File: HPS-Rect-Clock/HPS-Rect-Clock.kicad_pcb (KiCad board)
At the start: 2 copper layers, 140 x 90 mm, 58 parts, among them J1 Conn_01x06, J2 Power_inlet_vertical, J3 Conn_02x03_Odd_Even, SW1 Omron_B3F_SPST, SW2 Omron_B3F_SPST, SW3 Omron_B3F_SPST, SW4 Omron_B3F_SPST, SW5 Omron_B3F_SPST, U1 DS1307_DIP-8, U2 ATmega328-PU, U3 L7805, Y1 Crystal_16MHz, Y2 Crystal_32768Hz

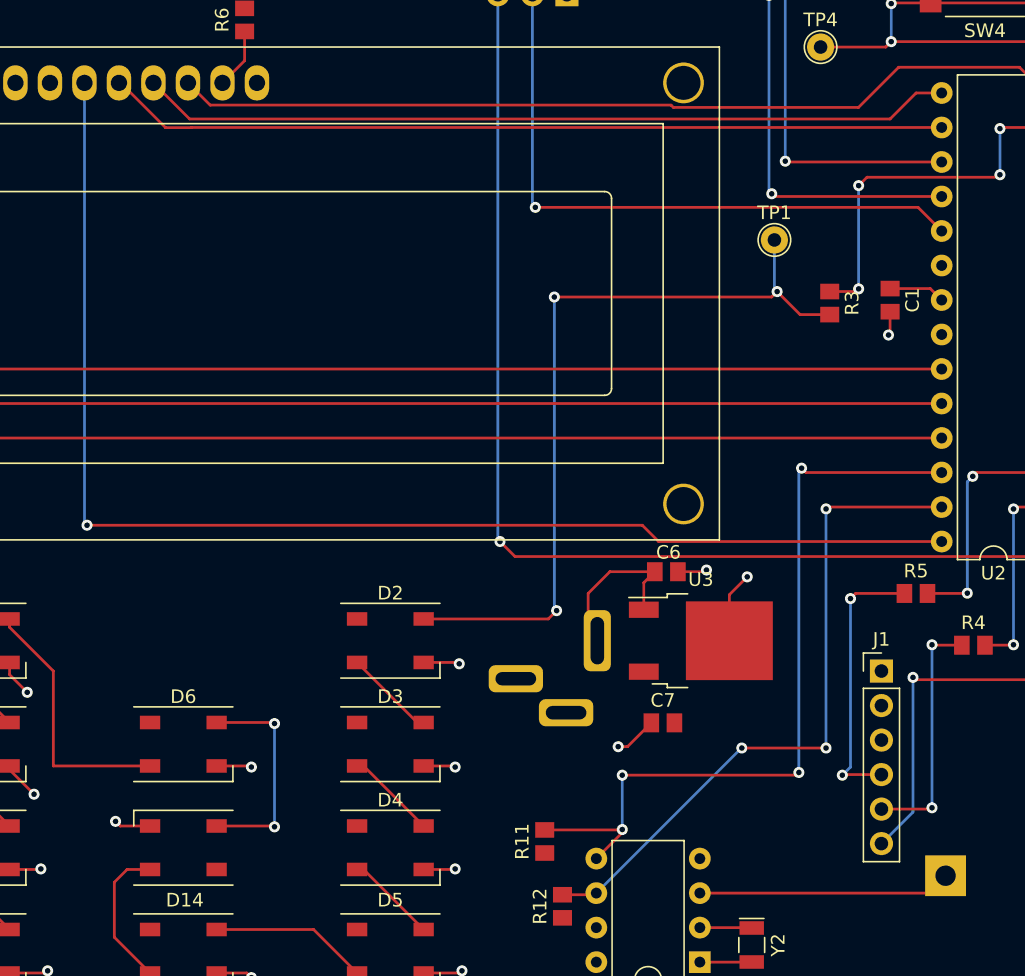
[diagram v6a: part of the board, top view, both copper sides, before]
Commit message: Updated Library and SDA and SCL pin
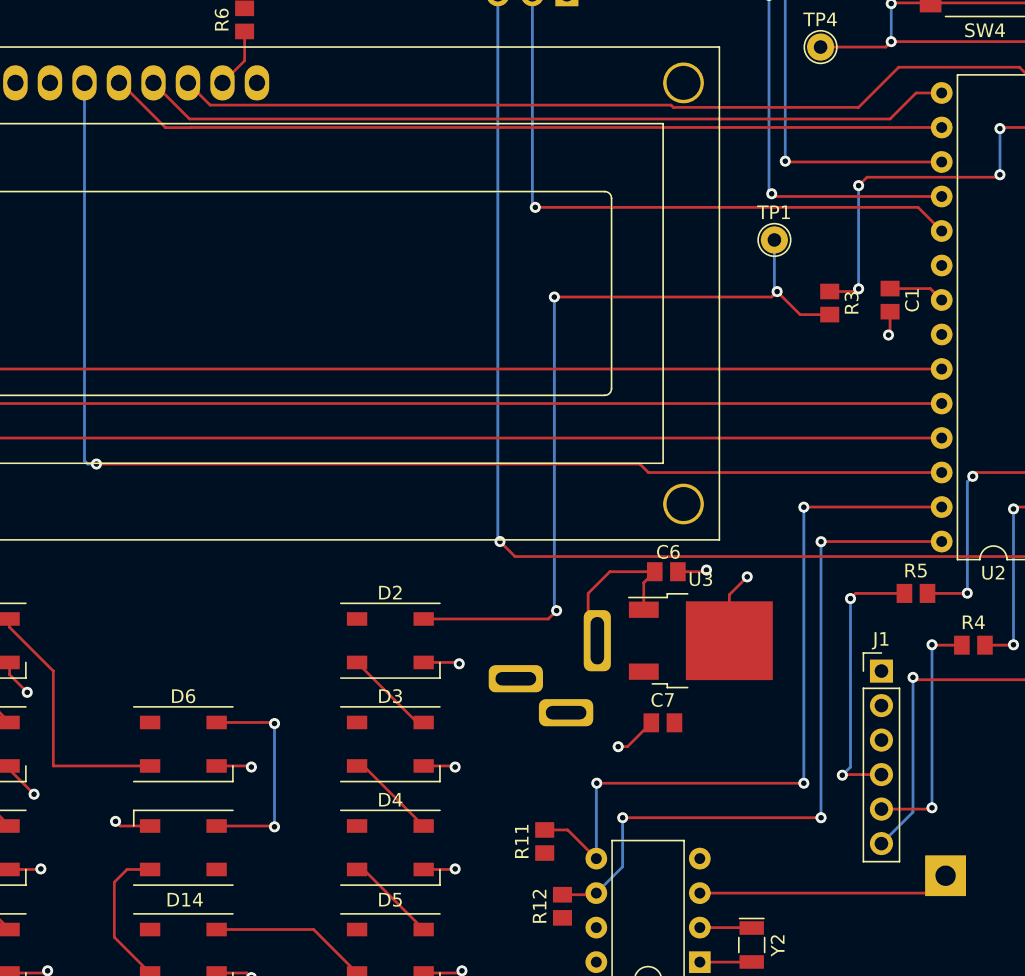
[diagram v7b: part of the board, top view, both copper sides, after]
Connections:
- U2 pad 26: SDA -> D4
- U2 pad 27: SCL -> SDA
- U2 pad 28: D4 -> SCL
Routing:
- net D4: track 96.1 -> 91.3 mm
- net SDA: track 58.7 -> 56.0 mm, vias 4 -> 3
- net SCL: track 50.0 -> 52.7 mm
